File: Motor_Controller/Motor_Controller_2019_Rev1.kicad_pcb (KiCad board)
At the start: 2 copper layers, 124.5 x 85.6 mm, 244 parts, among them Q12 Q_NMOS_DGS, Q13 Q_NMOS_DGS, Q14 Q_NMOS_DGS, Q15 Q_NMOS_DGS, Q16 Q_NMOS_DGS, Q17 Q_NMOS_DGS, Q4 Q_NMOS_DGS, Q5 Q_NMOS_DGS, Q6 Q_NMOS_DGS, Q7 Q_NMOS_DGS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

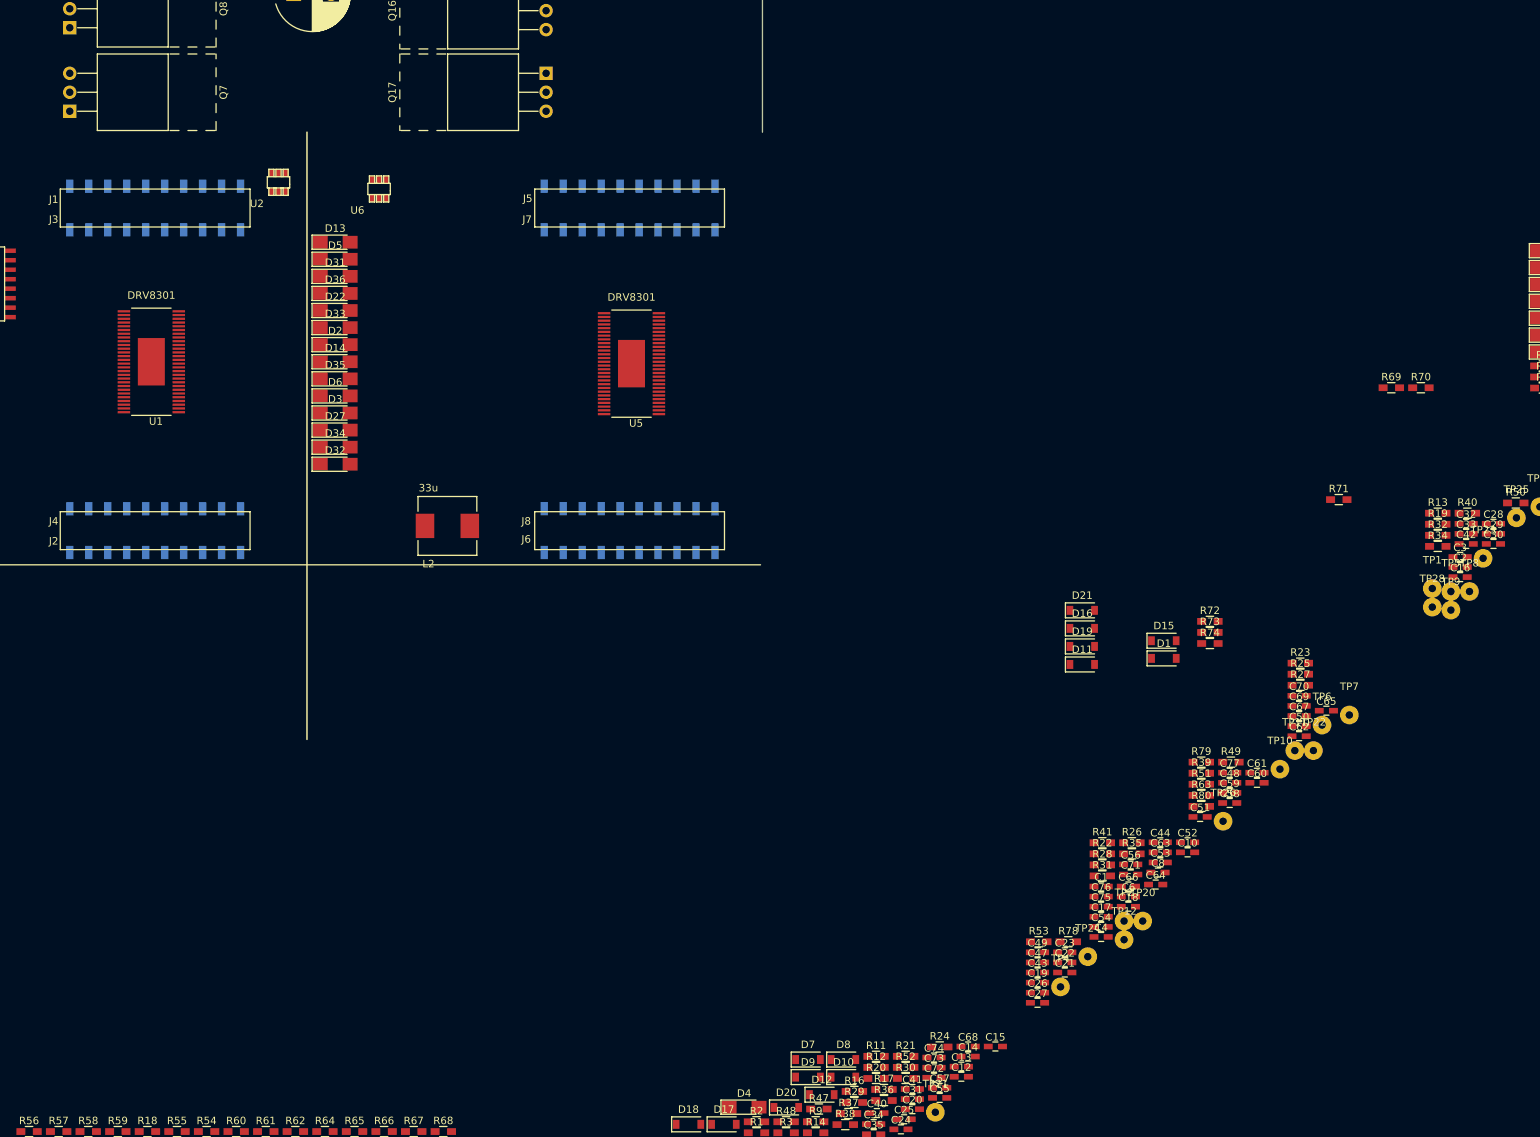
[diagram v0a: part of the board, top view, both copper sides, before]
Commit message: Make F28069m pinout top SMD
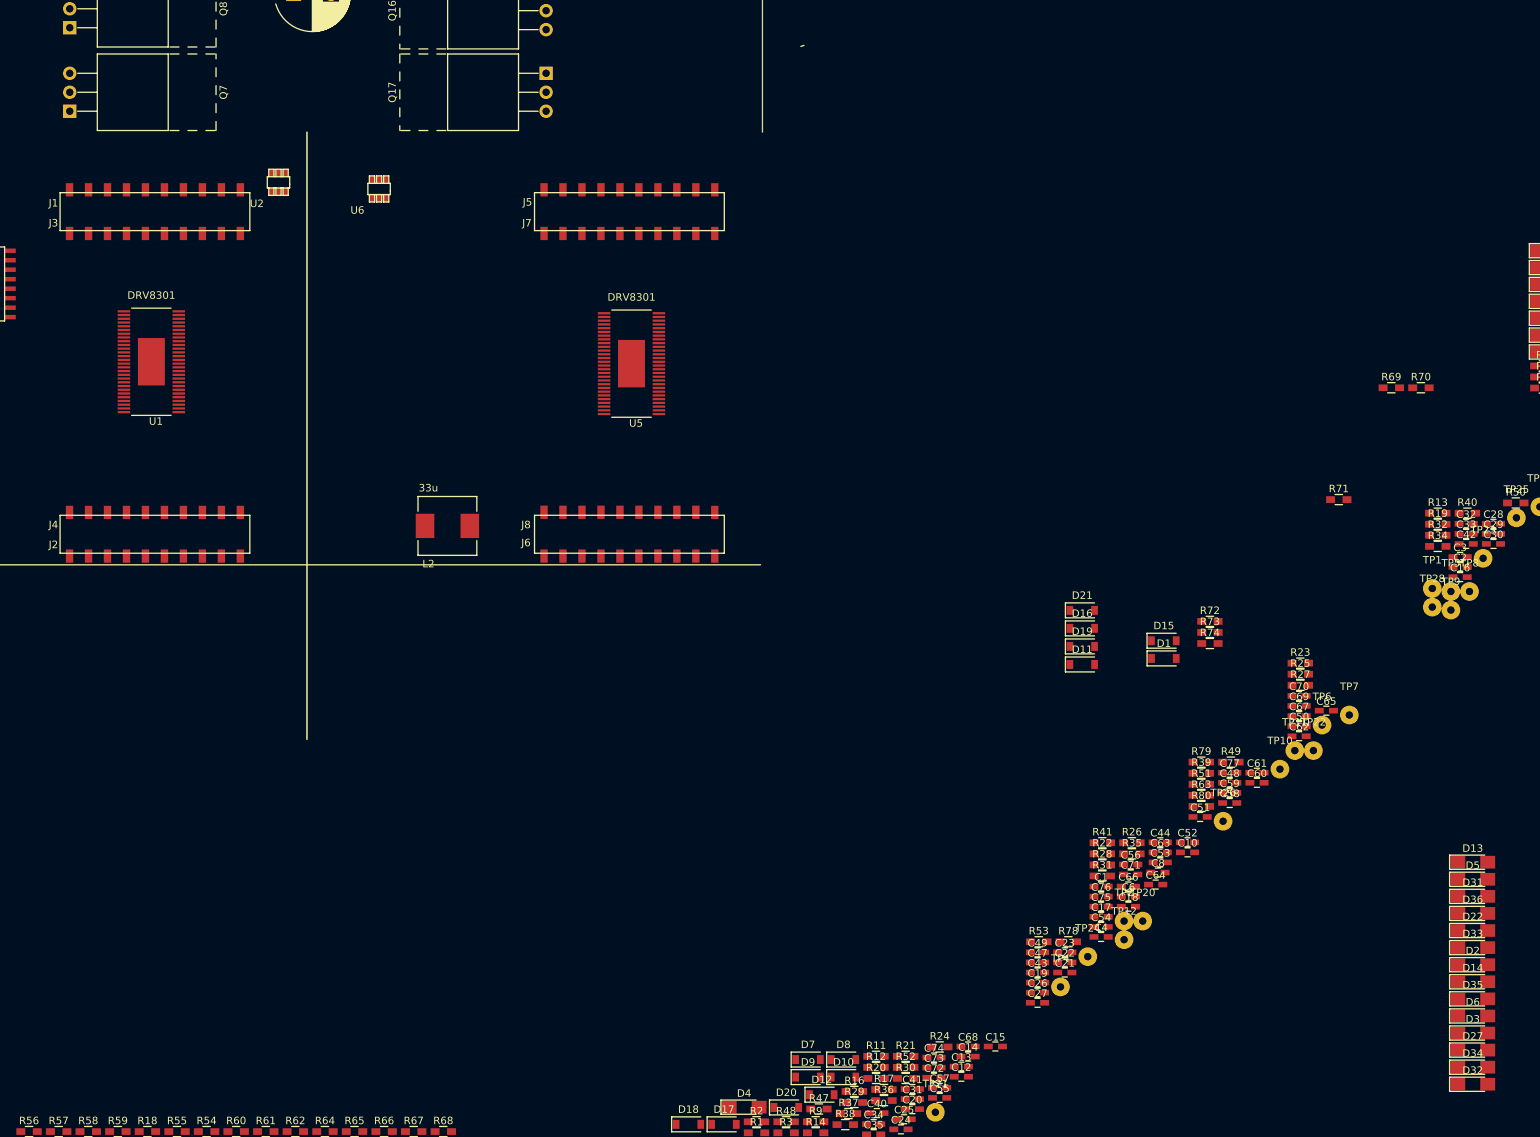
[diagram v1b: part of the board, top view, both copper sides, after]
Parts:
- U3: footprint MotorController_Hardware:LAUNCHXL_F28069M_Launchpad_FULL_Booster_SMD_Bottom -> MotorController_Hardware:LAUNCHXL_F28069M_Launchpad_FULL_Booster_SMD_Top
- moved D13 173.4 mm to (270.1, 124.4)
- moved D14 173.4 mm to (270.1, 140.4)
- moved D2 173.4 mm to (270.1, 138.1)
- moved D22 173.4 mm to (270.1, 133.5)
- moved D27 173.4 mm to (270.1, 149.5)
- moved D3 173.4 mm to (270.1, 147.2)
- moved D31 173.4 mm to (270.1, 129.0)
- moved D32 173.4 mm to (270.1, 154.1)
- moved D33 173.4 mm to (270.1, 135.8)
- moved D34 173.4 mm to (270.1, 151.8)
- moved D35 173.4 mm to (270.1, 142.7)
- moved D36 173.4 mm to (270.1, 131.2)
- moved D5 173.4 mm to (270.1, 126.7)
- moved D6 173.4 mm to (270.1, 145.0)
- moved U3 0.48 mm to (50.5, 83.0)
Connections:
- U1 pad 32: SP1_M1 -> (no net)
- U1 pad 55: Net-(U1-Pad55) -> (no net)
- U3 pad +5V: SL_B_M2 -> Net-(U3-Pad+5V)
- U3 pad A_A0: SDO_M1 -> SO1_M1
- U3 pad A_A1: DC_CAL_M1 -> (no net)
- U3 pad A_A2: Net-(U3-PadA_A2) -> BSENSE_M1
- U3 pad A_A3: SDO_M2 -> SO1_M2
- U3 pad A_A4: DC_CAL_M2 -> (no net)
- U3 pad A_A5: Net-(U3-PadA_A5) -> BSENSE_M2
- U3 pad A_A6: Net-(U3-PadA_A6) -> (no net)
- U3 pad A_A7: Net-(U3-PadA_A7) -> PVDDSENSE
- U3 pad A_B0: EN_GATE_M1 -> SO2_M1
- U3 pad A_B1: Net-(U3-PadA_B1) -> ASENSE_M1
- U3 pad A_B2: SDI_M1 -> CSENSE_M1
- U3 pad A_B3: EN_GATE_M2 -> SO2_M2
- U3 pad A_B4: Net-(U3-PadA_B4) -> ASENSE_M2
- U3 pad A_B5: SD1_M2 -> CSENSE_M2
- U3 pad A_B6: Net-(U3-PadA_B6) -> (no net)
- U3 pad A_B7: Net-(U3-PadA_B7) -> PVDDSENSE
- U3 pad DAC1: Net-(U3-PadDAC1) -> (no net)
- U3 pad DAC2: Net-(U3-PadDAC2) -> (no net)
- U3 pad DAC3: Net-(U3-PadDAC3) -> (no net)
- U3 pad DAC4: Net-(U3-PadDAC4) -> (no net)
- U3 pad NC: ASENSE_M2 -> Net-(U3-PadNC)
- U3 pad P_13: Net-(U3-PadP_13) -> (no net)
- U3 pad P_16: CSENSE_M1 -> SDI_M1
- U3 pad P_17: SO1_M1 -> SDO_M1
- U3 pad P_19: Net-(U3-PadP_19) -> (no net)
- U3 pad P_21: Net-(U3-PadP_21) -> (no net)
- U3 pad P_22: Net-(U3-PadP_22) -> (no net)
- U3 pad P_24: CSENSE_M2 -> (no net)
- U3 pad P_25: SO1_M2 -> SDO_M2
- U3 pad P_26: PVDDSENSE -> (no net)
- U3 pad P_27: Net-(U3-PadP_27) -> (no net)
- U3 pad P_44: PVDDSENSE -> (no net)
- U3 pad P_50: SO2_M1 -> EN_GATE_M1
- U3 pad P_51: Net-(U3-PadP_51) -> DC_CAL_M1
- U3 pad P_52: SO2_M2 -> EN_GATE_M2
- U3 pad P_53: Net-(U3-PadP_53) -> DC_CAL_M2
- U3 pad P_55: Net-(U3-PadP_55) -> (no net)
- U3 pad P_56: Net-(U3-PadP_56) -> (no net)
- U3 pad Rese: BSENSE_M2 -> Net-(U3-PadRese)
- U5 pad 55: Net-(U5-Pad55) -> (no net)
- U5 pad 9: SDI_M2 -> (no net)

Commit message: Fixed netlist naming for GND
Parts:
- removed Conn2: PVDD_M1_PP, MRDT_Connectors:Anderson_1_Horisontal
- removed Conn7: PVDD_M2_PP, MRDT_Connectors:Anderson_1_Horisontal
- Conn3: value GND_M1_PP -> AndersonPP; footprint MRDT_Connectors:Anderson_1_Horisontal -> MRDT_Connectors:Anderson_2_Vertical
- Conn8: value GND_M2_PP -> AndersonPP; footprint MRDT_Connectors:Anderson_1_Horisontal -> MRDT_Connectors:Anderson_2_Vertical
- moved U2 137.7 mm to (247.9, 27.4)
- moved U4 107.4 mm to (-31.3, 16.2)
- moved U6 94.6 mm to (218.0, 25.3)
- moved Conn1 83.9 mm to (-21.6, 53.1)
- moved U5 62.3 mm to (219.7, 54.3)
- moved U1 61.7 mm to (33.1, 71.3)
- moved L1 54.4 mm to (17.6, 97.4)
- moved Conn3 50.1 mm to (45.8, -80.4)
- moved L2 43.2 mm to (120.4, 120.8)
- moved Conn4 42.5 mm to (21.8, -15.9)
- moved Conn5 42.5 mm to (21.8, -8.00)
- moved Conn6 42.4 mm to (21.8, -0.13)
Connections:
- C1 pad 2: SL_B_M2 -> GND
- C10 pad 2: SL_B_M2 -> GND
- C12 pad 2: SL_B_M2 -> GND
- C14 pad 2: SL_B_M2 -> GND
- C15 pad 2: SL_B_M2 -> GND
- C2 pad 2: SL_B_M2 -> GND
- C21 pad 2: SL_B_M2 -> GND
- C22 pad 1: SL_B_M2 -> GND
- C23 pad 1: SL_B_M2 -> GND
- C24 pad 1: SL_B_M2 -> GND
- C25 pad 1: SL_B_M2 -> GND
- C26 pad 1: SL_B_M2 -> GND
- C27 pad 1: SL_B_M2 -> GND
- C28 pad 2: SL_B_M2 -> GND
- C29 pad 2: SL_B_M2 -> GND
- C3 pad 2: SL_B_M2 -> GND
- C30 pad 1: PVDD -> PVDD_M1
- C30 pad 2: SL_B_M2 -> GND
- C31 pad 1: PVDD -> PVDD_M1
- C31 pad 2: SL_B_M2 -> GND
- C32 pad 1: PVDD -> PVDD_M1
- C32 pad 2: SL_B_M2 -> GND
- C33 pad 2: SL_B_M2 -> GND
- C34 pad 2: SL_B_M2 -> GND
- C35 pad 2: SL_B_M2 -> GND
- C36 pad 1: PVDD -> PVDD_M1
- C36 pad 2: SL_B_M2 -> GND
- C37 pad 1: PVDD -> PVDD_M1
- C37 pad 2: SL_B_M2 -> GND
- C38 pad 1: PVDD -> PVDD_M1
- C38 pad 2: SL_B_M2 -> GND
- C39 pad 1: PVDD -> PVDD_M2
- C39 pad 2: SL_B_M2 -> GND
- C4 pad 2: SL_B_M2 -> GND
- C40 pad 1: SL_B_M2 -> GND
- C41 pad 2: SL_B_M2 -> GND
- C42 pad 2: SL_B_M2 -> GND
- C45 pad 2: SL_B_M2 -> GND
- C47 pad 2: SL_B_M2 -> GND
- C49 pad 2: SL_B_M2 -> GND
- C5 pad 1: PVDD -> PVDD_M2
- C5 pad 2: SL_B_M2 -> GND
- C50 pad 2: SL_B_M2 -> GND
- C51 pad 2: SL_B_M2 -> GND
- C52 pad 2: SL_B_M2 -> GND
- C53 pad 2: SL_B_M2 -> GND
- C54 pad 2: SL_B_M2 -> GND
- C55 pad 2: SL_B_M2 -> GND
- C56 pad 2: SL_B_M2 -> GND
- C57 pad 2: SL_B_M2 -> GND
- C59 pad 2: SL_B_M2 -> GND
- C6 pad 2: SL_B_M2 -> GND
- C64 pad 1: SL_B_M2 -> GND
- C65 pad 1: SL_B_M2 -> GND
- C66 pad 1: SL_B_M2 -> GND
- C67 pad 1: SL_B_M2 -> GND
- C68 pad 1: SL_B_M2 -> GND
- C69 pad 1: SL_B_M2 -> GND
- C7 pad 1: PVDD -> PVDD_M2
- C7 pad 2: SL_B_M2 -> GND
- C70 pad 2: SL_B_M2 -> GND
- C71 pad 2: SL_B_M2 -> GND
- C72 pad 1: PVDD -> PVDD_M2
- C72 pad 2: SL_B_M2 -> GND
- C73 pad 1: PVDD -> PVDD_M2
- C73 pad 2: SL_B_M2 -> GND
- C74 pad 1: PVDD -> PVDD_M2
- C74 pad 2: SL_B_M2 -> GND
- C75 pad 2: SL_B_M2 -> GND
- C76 pad 2: SL_B_M2 -> GND
- C77 pad 2: SL_B_M2 -> GND
- C8 pad 2: SL_B_M2 -> GND
- C9 pad 2: SL_B_M2 -> GND
- Conn1 pad 5: SL_B_M2 -> GND
- Conn3 pad 1: SL_B_M2 -> GND
- Conn8 pad 1: SL_B_M2 -> GND
- D1 pad 2: SL_B_M2 -> GND
- D12 pad 2: SL_B_M2 -> GND
- D15 pad 2: SL_B_M2 -> GND
- D21 pad 2: SL_B_M2 -> GND
- Q12 pad 1: PVDD -> PVDD_M2
- Q14 pad 1: PVDD -> PVDD_M2
- Q16 pad 1: PVDD -> PVDD_M2
- Q17 pad 3: SL_B_M2 -> GND
- Q4 pad 1: PVDD -> PVDD_M1
- Q6 pad 1: PVDD -> PVDD_M1
- Q8 pad 1: PVDD -> PVDD_M1
- Q9 pad 3: SL_B_M2 -> GND
- R10 pad 1: SL_B_M2 -> GND
- R13 pad 1: SL_B_M2 -> GND
- R14 pad 2: SL_B_M2 -> GND
- R16 pad 2: SL_B_M2 -> GND
- R17 pad 1: SL_B_M2 -> GND
- R18 pad 2: SL_B_M2 -> GND
- R19 pad 2: SL_B_M2 -> GND
- R21 pad 1: SL_B_M2 -> GND
- R28 pad 2: SL_B_M2 -> GND
- R29 pad 2: SL_B_M2 -> GND
- R31 pad 2: SL_B_M2 -> GND
- R33 pad 2: SL_B_M2 -> GND
- R35 pad 2: SL_B_M2 -> GND
- R36 pad 1: SL_B_M2 -> GND
- R37 pad 1: SL_B_M2 -> GND
- R41 pad 2: SL_B_M2 -> GND
- R43 pad 2: SL_B_M2 -> GND
- R44 pad 2: SL_B_M2 -> GND
- R47 pad 2: SL_B_M2 -> GND
- R48 pad 2: SL_B_M2 -> GND
- R5 pad 2: SL_B_M2 -> GND
- R56 pad 2: SL_B_M2 -> GND
- R57 pad 2: SL_B_M2 -> GND
- R59 pad 2: SL_B_M2 -> GND
- R6 pad 2: SL_B_M2 -> GND
- R61 pad 2: SL_B_M2 -> GND
- R63 pad 2: SL_B_M2 -> GND
- R64 pad 1: SL_B_M2 -> GND
- R65 pad 1: SL_B_M2 -> GND
- R66 pad 1: SL_B_M2 -> GND
- R67 pad 1: SL_B_M2 -> GND
- R68 pad 1: SL_B_M2 -> GND
- R69 pad 1: SL_B_M2 -> GND
- R7 pad 1: SL_B_M2 -> GND
- R70 pad 1: SL_B_M2 -> GND
- R71 pad 1: SL_B_M2 -> GND
- R72 pad 1: SL_B_M2 -> GND
- R73 pad 1: SL_B_M2 -> GND
- R74 pad 1: SL_B_M2 -> GND
- R75 pad 1: SL_B_M2 -> GND
- R76 pad 1: SL_B_M2 -> GND
- R77 pad 1: SL_B_M2 -> GND
- R78 pad 2: SL_B_M2 -> GND
- R8 pad 2: SL_B_M2 -> GND
- R80 pad 2: SL_B_M2 -> GND
- R9 pad 1: SL_B_M2 -> GND
- U1 pad 28: SL_B_M2 -> GND
- U1 pad 30: SL_B_M2 -> GND
- U1 pad 32: (no net) -> GND
- U1 pad 34: SL_B_M2 -> GND
- U1 pad 57: SL_B_M2 -> GND
- U2 pad 5: SL_B_M2 -> GND
- U4 pad 15: SL_B_M2 -> GND
- U5 pad 28: SL_B_M2 -> GND
- U5 pad 30: SL_B_M2 -> GND
- U5 pad 32: SL_B_M2 -> GND
- U5 pad 34: SL_B_M2 -> GND
- U5 pad 57: SL_B_M2 -> GND
- U6 pad 5: SL_B_M2 -> GND

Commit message: Updated Layout
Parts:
- C15, C16, C47, C48: footprint Capacitors_SMD:C_0603_HandSoldering -> Capacitors_SMD:C_1206_HandSoldering
- C30, C31, C32, C72, C73, C74: footprint Capacitors_SMD:C_0603_HandSoldering -> Capacitors_SMD:C_1206_HandSoldering; moved to B.Cu
- C71, Q12, Q13, Q14, Q15, Q16, Q17, Q4, Q5, Q6, Q7, Q8, Q9: moved to B.Cu
- R28, R29, R56, R57: footprint Resistors_SMD:R_0603_HandSoldering -> Resistors_SMD:R_1206_HandSoldering
- moved R28 209.5 mm to (90.6, -39.6), turned to 180 degrees
- moved C31 207.1 mm to (108.0, -31.8), turned to 90 degrees
- moved C73 200.4 mm to (117.7, -31.8), turned to 270 degrees
- moved R29 199.8 mm to (90.6, -18.3), turned to 180 degrees
- moved R56 193.3 mm to (135.1, -23.9)
- moved C32 184.4 mm to (108.0, -10.3), turned to 90 degrees
- moved C16 182.7 mm to (95.0, 28.6), turned to 180 degrees
- moved C72 182.3 mm to (117.7, -10.4), turned to 270 degrees
- moved C30 179.5 mm to (108.0, 11.0), turned to 90 degrees
- moved R57 171.8 mm to (135.1, -2.54)
- moved R14 162.0 mm to (88.3, 28.6), turned to 180 degrees
- moved C74 161.1 mm to (117.7, 10.8), turned to 270 degrees
- moved C15 157.4 mm to (104.8, 28.6)
- moved C47 141.6 mm to (121.9, 28.4), turned to 180 degrees
- moved C48 136.0 mm to (131.7, 28.4)
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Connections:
- U3 pad GND: Net-(U3-PadGND) -> GND
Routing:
- net GND: track 0.00 -> 27.3 mm
- net PVDD_M1: track 0.00 -> 11.6 mm
- net PVDD_M2: track 0.00 -> 11.4 mm
- net SL_B_M1: track 0.00 -> 3.68 mm
- net SL_A_M1: track 0.00 -> 3.68 mm
- net SL_B_M2: track 0.00 -> 3.68 mm
- net SL_A_M2: track 0.00 -> 3.68 mm
- net Net-(C16-Pad2): track 0.00 -> 3.66 mm
- net Net-(C48-Pad2): track 0.00 -> 3.24 mm
- added copper zone on F.Cu, net GND
- added copper zone on B.Cu, net PVDD_M1
- added copper zone on B.Cu, net PVDD_M2
- added copper zone on F.Cu, net SH_A_M1
- added copper zone on F.Cu, net SH_A_M2
- added copper zone on F.Cu, net SH_B_M1
- added copper zone on F.Cu, net SH_B_M2
- added copper zone on F.Cu, net SH_C_M1
- added copper zone on F.Cu, net SH_C_M2
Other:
- board size 124.5 x 85.6 mm -> 124.4 x 86.1 mm

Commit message: Modified layout
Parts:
- moved Conn1 86.4 mm to (63.6, 38.9)
- moved U4 66.5 mm to (56.9, 53.2), turned to 90 degrees
- moved U1 62.9 mm to (94.6, 57.9), turned to 90 degrees
- moved U5 62.8 mm to (157.1, 59.3), turned to 90 degrees
- moved L1 34.6 mm to (33.7, 66.7)

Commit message: routed primary control traces
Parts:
- C6: footprint Capacitors_SMD:C_0603_HandSoldering -> Capacitor_THT:CP_Radial_D6.3mm_P2.50mm
- U1: value DRV8301 -> DCA56_6P35X3P61
- moved C3 302.8 mm to (-32.0, 45.1)
- moved R19 274.0 mm to (-8.59, 75.1)
- moved C2 271.8 mm to (-3.36, 78.2)
- moved C1 263.9 mm to (-32.0, 50.4)
- moved R55 253.5 mm to (350.1, 164.2)
- moved R58 253.5 mm to (338.3, 164.2)
- moved R59 253.5 mm to (342.2, 164.2)
- moved R61 253.5 mm to (362.0, 164.2)
- moved R64 253.5 mm to (369.9, 164.2)
- moved R65 253.5 mm to (373.9, 164.2)
- moved R67 253.5 mm to (381.8, 164.2)
- moved R54 253.5 mm to (354.1, 164.2)
- moved R62 253.5 mm to (366.0, 164.2)
- moved R66 253.5 mm to (377.9, 164.2)
- moved R68 253.5 mm to (385.8, 164.2)
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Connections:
- C10 pad 1: PVDD -> PVDD_M1
- C2 pad 1: PVDD -> PVDD_M1
- C4 pad 1: PVDD -> PVDD_M1
- C51 pad 1: PVDD -> PVDD_M2
- C53 pad 1: PVDD -> PVDD_M2
- C55 pad 1: PVDD -> PVDD_M2
- C56 pad 1: PVDD -> PVDD_M2
- C8 pad 1: PVDD -> PVDD_M1
- D3 pad 2: PVDD -> (no net)
- U1 pad 29: PVDD -> PVDD_M1
- U1 pad 53: PVDD -> PVDD_M1
- U1 pad 54: PVDD -> PVDD_M1
- U5 pad 29: PVDD -> PVDD_M2
- U5 pad 53: PVDD -> PVDD_M2
- U5 pad 54: PVDD -> PVDD_M2
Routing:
- net SL_A_M1: track 3.68 -> 180.0 mm, vias 0 -> 2
- net SL_B_M1: track 3.68 -> 152.9 mm, vias 0 -> 2
- net SH_A_M1: track 0.00 -> 125.4 mm, vias 0 -> 1
- net Net-(D8-Pad1): track 0.00 -> 124.3 mm, vias 0 -> 1
- net Net-(D7-Pad1): track 0.00 -> 110.1 mm, vias 0 -> 1
- net Net-(D10-Pad1): track 0.00 -> 102.7 mm, vias 0 -> 1
- net SH_B_M1: track 0.00 -> 102.3 mm, vias 0 -> 1
- net Net-(D9-Pad1): track 0.00 -> 87.7 mm, vias 0 -> 1
- net Net-(D12-Pad1): track 0.00 -> 83.0 mm, vias 0 -> 1
- net SH_C_M1: track 0.00 -> 82.9 mm, vias 0 -> 1
- net GND: track 27.3 -> 107.5 mm, vias 0 -> 1
- net Net-(D11-Pad1): track 0.00 -> 67.3 mm, vias 0 -> 1
- net PVDD_M1: track 11.6 -> 67.2 mm, vias 0 -> 1
- net GH_C_M1: track 0.00 -> 10.2 mm
- net GH_A_M1: track 0.00 -> 10.1 mm
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
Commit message: Began work on signal traces
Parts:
- moved R2 103.7 mm to (73.4, 50.6)
- moved R1 98.4 mm to (73.4, 52.2)
- moved C27 98.0 mm to (83.2, 67.6), turned to 180 degrees
- moved R3 89.6 mm to (73.4, 49.0)
- moved C25 85.5 mm to (73.5, 59.1)
- moved R19 84.7 mm to (73.4, 53.9), turned to 180 degrees
- moved R6 82.1 mm to (73.4, 57.5), turned to 180 degrees
- moved R20 78.3 mm to (78.2, 49.8), turned to 270 degrees
- moved C14 77.3 mm to (68.8, 69.1), turned to 180 degrees
- moved R4 76.4 mm to (73.4, 47.4)
- moved C12 74.5 mm to (68.8, 70.8), turned to 180 degrees
- moved R5 74.2 mm to (73.4, 45.8), turned to 180 degrees
- moved C26 70.4 mm to (73.0, 67.4)
- moved C23 69.5 mm to (79.8, 45.3), turned to 270 degrees
- moved C24 67.5 mm to (78.2, 45.3), turned to 270 degrees
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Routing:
- net PVDD_M1: track 67.2 -> 77.2 mm
- net Net-(C23-Pad2): track 0.00 -> 9.71 mm
- net SCLK_M1: track 0.00 -> 9.33 mm
- net SDI_M1: track 0.00 -> 9.20 mm
- net NSCS_M1: track 0.00 -> 9.20 mm
- net SDO_M1: track 0.00 -> 9.08 mm
- net Net-(R4-Pad2): track 0.00 -> 8.72 mm
- net Net-(C17-Pad1): track 0.00 -> 8.23 mm
- net Net-(R19-Pad1): track 0.00 -> 6.63 mm
- net PWRGD_M1: track 0.00 -> 6.33 mm
- net Net-(C17-Pad2): track 0.00 -> 6.12 mm
- net DC_CAL_M1: track 0.00 -> 6.02 mm
- net Net-(C25-Pad2): track 0.00 -> 5.86 mm
- net NOCTW_M1: track 0.00 -> 5.63 mm
- net NFAULT_M1: track 0.00 -> 5.36 mm
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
